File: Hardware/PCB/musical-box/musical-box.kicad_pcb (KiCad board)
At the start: 4 copper layers, 70 x 60 mm, 190 parts, among them J1 power, J201 PSU, J202 Jack-DC, J203 BATT, J401 SPI Display, J402 Rotary Encoder 1, J403 I2C Display, J404 Rotary Encoder 2, J405 WS2812, J501 spk_out, J502 aux in, J503 line in, P201 USB_C, P202 ICT-Point, P203 ICT-Point, P204 ICT-Point, Q201 IRFHM9331, Q204 IRF9362, Q301 BC846BDW1, SW301 boot, SW302 reset, U201 STUSB4500QTR, U202 MP2615, U203 TPS56339, U204 TLV75733PDBV, U205 TLV75733PDBV, U206 TLV803EC30DBZR, U301 CH340C, U302 ESP32-WROVER, U401 PCF8574ATS, U501 SPH0644HM4H-1, U502 SPH0644HM4H-1, U503 TAS5754MDCA

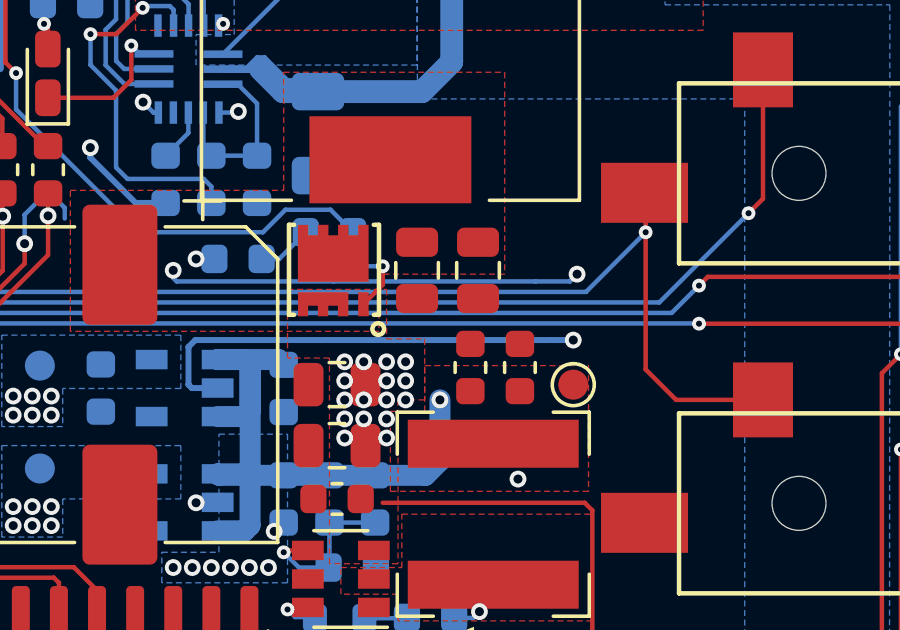
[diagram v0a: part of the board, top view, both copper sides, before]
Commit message: Fix error in schematic
The P-Channel MOSFet was connected in the wrong way, preventing the shutoff circuit from working properly
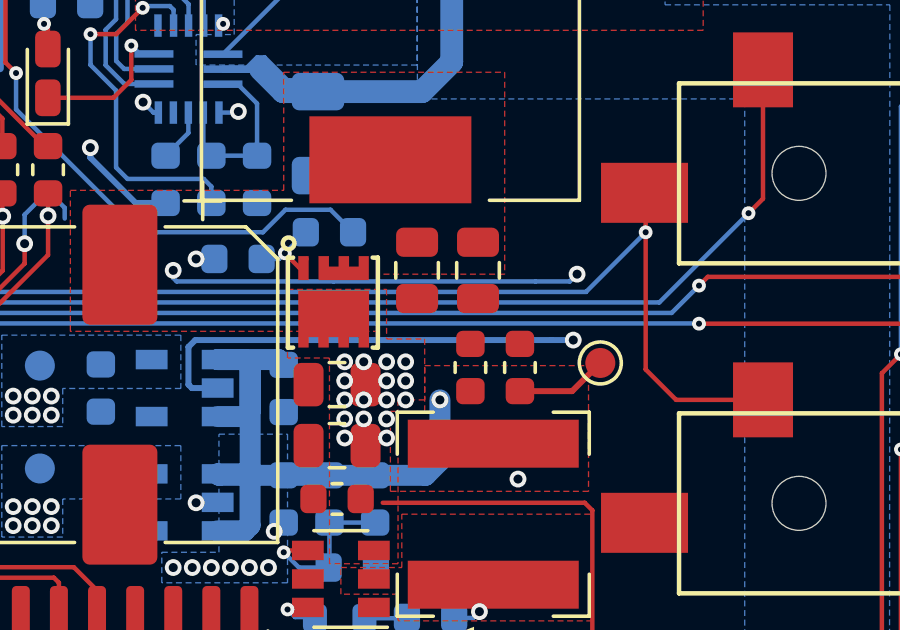
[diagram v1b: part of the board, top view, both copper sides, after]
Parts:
- R409: value 46.4k -> 46,4k
- moved P204 1.16 mm to (401.8, 155.3)
- moved Q201 0.29 mm to (392.9, 152.9), turned to 270 degrees
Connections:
- D202 pad 2: (no net) -> Net-(D202-Pad2)
- P201 pad A8: (no net) -> Net-(P201-PadA8)
- P201 pad B8: (no net) -> Net-(P201-PadB8)
- Q201 pad 2: +15V -> Net-(C201-Pad2)
- Q201 pad 3: Net-(C201-Pad2) -> +15V
- U201 pad 14: (no net) -> Net-(U201-Pad14)
- U201 pad 15: (no net) -> Net-(U201-Pad15)
- U201 pad 17: (no net) -> Net-(U201-Pad17)
- U201 pad 20: (no net) -> Net-(U201-Pad20)
- U201 pad 3: (no net) -> Net-(U201-Pad3)
- U202 pad 12: (no net) -> Net-(U202-Pad12)
- U203 pad 5: (no net) -> Net-(U203-Pad5)
- U301 pad 10: (no net) -> Net-(U301-Pad10)
- U301 pad 11: (no net) -> Net-(U301-Pad11)
- U301 pad 12: (no net) -> Net-(U301-Pad12)
- U301 pad 15: (no net) -> Net-(U301-Pad15)
- U301 pad 7: (no net) -> Net-(U301-Pad7)
- U301 pad 8: (no net) -> Net-(U301-Pad8)
- U301 pad 9: (no net) -> Net-(U301-Pad9)
- U302 pad 17: (no net) -> Net-(U302-Pad17)
- U302 pad 18: (no net) -> Net-(U302-Pad18)
- U302 pad 19: (no net) -> Net-(U302-Pad19)
- U302 pad 20: (no net) -> Net-(U302-Pad20)
- U302 pad 21: (no net) -> Net-(U302-Pad21)
- U302 pad 22: (no net) -> Net-(U302-Pad22)
- U401 pad 13: (no net) -> Net-(U401-Pad13)
- U401 pad 18: (no net) -> Net-(U401-Pad18)
- U401 pad 19: (no net) -> Net-(U401-Pad19)
- U401 pad 20: (no net) -> Net-(U401-Pad20)
- U401 pad 3: (no net) -> Net-(U401-Pad3)
- U401 pad 8: (no net) -> Net-(U401-Pad8)
- U503 pad 19: (no net) -> /Audio Output/GPIO1
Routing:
- net Net-(Q201-Pad1): track 6.92 -> 2.72 mm
- net +5V: track 82.1 -> 85.1 mm

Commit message: Addendum to 9e53ee1
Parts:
- C218, C222, C505, C506, C527, C528: value 22u -> 10u
- L203: value XAL6030-332MEB -> XAL6030-562
- R219: value 30.9k -> 52.3k
- R222, R312: value 10k -> 1k
- R302, R303: value 470R -> 220R
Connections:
- Q204 pad 1: Net-(Q204-Pad1) -> Net-(C204-Pad1)
- Q204 pad 3: Net-(Q204-Pad1) -> Net-(C204-Pad1)
- R204 pad 1: Net-(Q204-Pad1) -> Net-(C204-Pad1)
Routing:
- net Net-(C204-Pad1): track 1.11 -> 8.51 mm, vias 1 -> 2
- net Net-(Q204-Pad1): track 2.05 -> 0.00 mm, vias 1 -> 0
- net GND: track 309.4 -> 310.8 mm
- added copper zone on F.Cu, net Net-(C204-Pad1)
- removed copper zone on F.Cu, net Net-(Q204-Pad1)

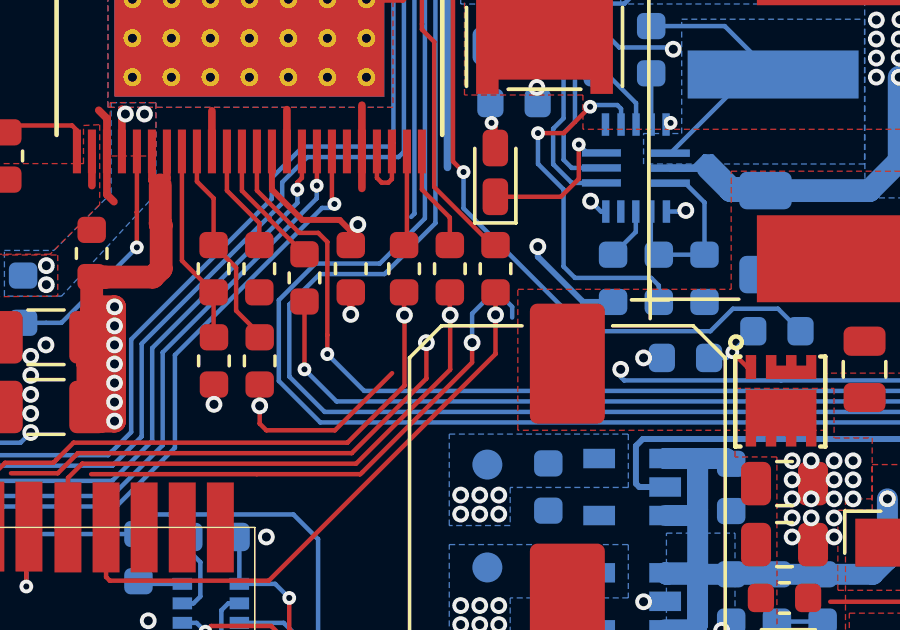
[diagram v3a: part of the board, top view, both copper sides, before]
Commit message: Remove needless vias
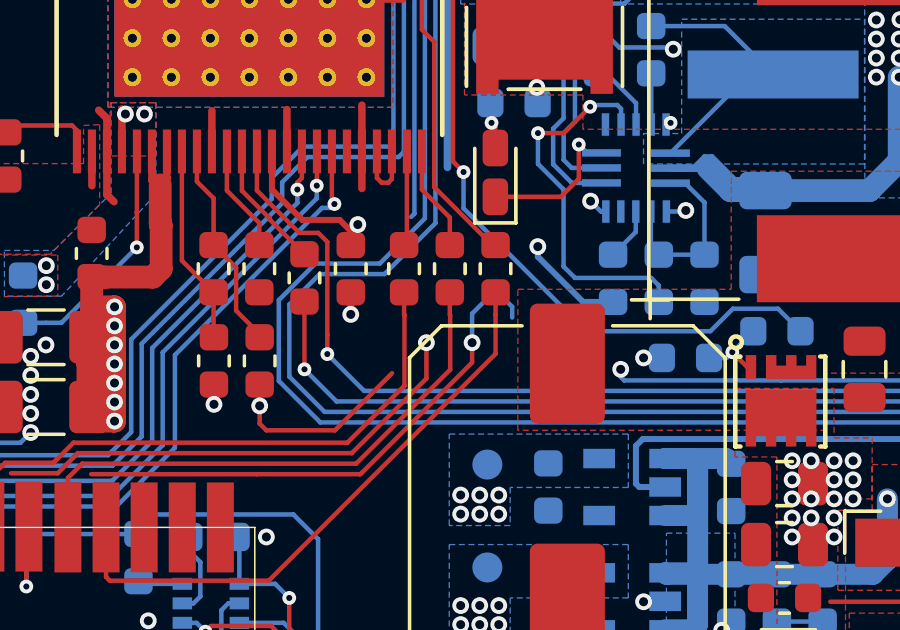
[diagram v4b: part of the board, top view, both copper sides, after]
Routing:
- net /Microcontroller/IO15: vias 1 -> 0
- net /Microcontroller/IO04: vias 1 -> 0
- net /Microcontroller/IO02: vias 1 -> 0

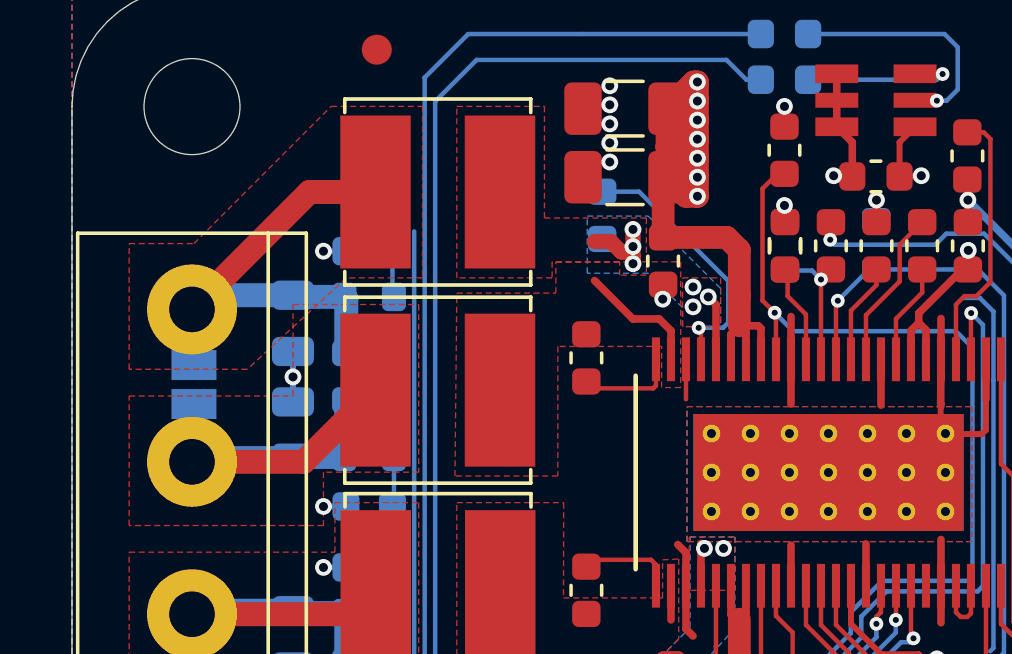
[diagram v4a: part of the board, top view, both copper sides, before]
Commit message: Bugfix: Fix speaker B connection to make the output work
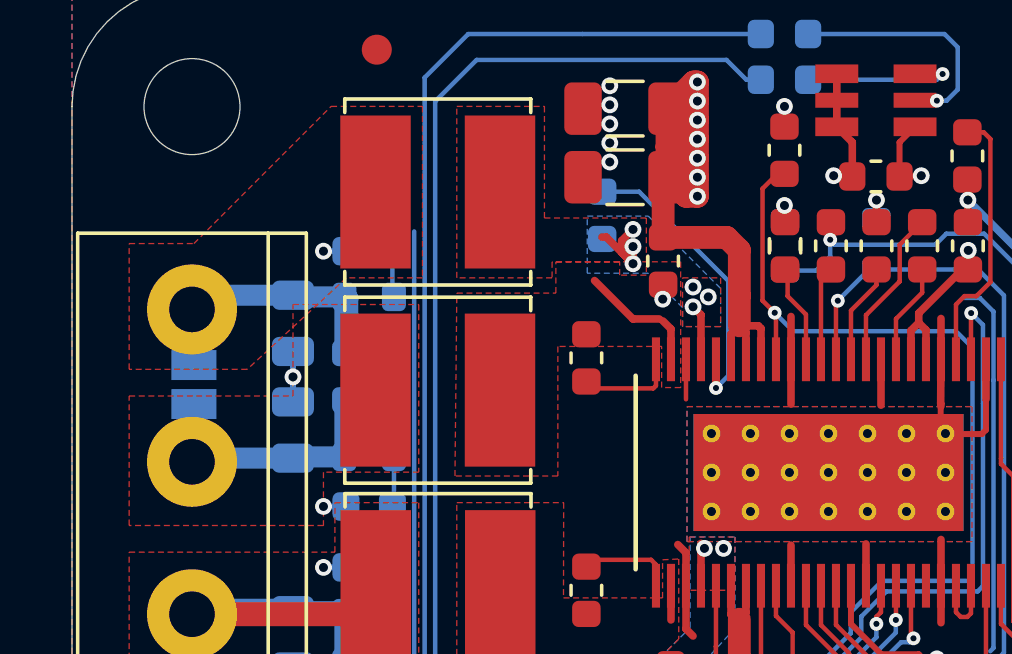
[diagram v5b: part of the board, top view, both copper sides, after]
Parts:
- R508: value 46.4k -> 10k
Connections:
- C515 pad 1: /Audio Output/SPKB_OUT+ -> /Audio Output/SPKB_OUT-
- C516 pad 1: /Audio Output/OUT2+ -> /Audio Output/OUT2-
- C519 pad 1: /Audio Output/OUT2+ -> /Audio Output/OUT2-
- C519 pad 2: /Audio Output/OUT2- -> /Audio Output/OUT2+
- C520 pad 1: /Audio Output/SPKB_OUT- -> /Audio Output/SPKB_OUT+
- C523 pad 1: /Audio Output/OUT2- -> /Audio Output/OUT2+
- C525 pad 1: /Audio Output/SPK_INB+ -> Net-(C525-Pad1)
- C525 pad 2: Net-(C525-Pad2) -> /Audio Output/SPK_INB+
- J501 pad 3: /Audio Output/OUT2+ -> /Audio Output/OUT2-
- J501 pad 4: /Audio Output/OUT2- -> /Audio Output/OUT2+
- J502 pad R1: Net-(C525-Pad2) -> /Audio Output/SPK_INB+
- JP4 pad 1: /Audio Output/OUT2+ -> /Audio Output/OUT2-
- JP4 pad 2: /Audio Output/OUT2- -> /Audio Output/OUT2+
- L503 pad 1: /Audio Output/SPKB_OUT+ -> /Audio Output/SPKB_OUT-
- L503 pad 2: /Audio Output/OUT2+ -> /Audio Output/OUT2-
- L504 pad 1: /Audio Output/SPKB_OUT- -> /Audio Output/SPKB_OUT+
- L504 pad 2: /Audio Output/OUT2- -> /Audio Output/OUT2+
- R510 pad 2: /Audio Output/OUT2+ -> /Audio Output/OUT2-
- R511 pad 2: /Audio Output/OUT2- -> /Audio Output/OUT2+
- U503 pad 37: /Audio Output/SPK_INB+ -> Net-(C525-Pad1)
- U503 pad 44: /Audio Output/SPKB_OUT- -> Net-(C520-Pad2)
- U503 pad 45: Net-(C520-Pad2) -> /Audio Output/SPKB_OUT+
- U503 pad 47: /Audio Output/SPKB_OUT+ -> /Audio Output/SPKB_OUT-
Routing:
- net Net-(C525-Pad2): track 68.0 -> 0.00 mm, vias 2 -> 0
- net /Audio Output/SPK_INB+: track 4.45 -> 70.3 mm, vias 1 -> 2
- net /Audio Output/OUT2-: track 16.8 -> 9.01 mm
- net /Audio Output/OUT2+: track 16.1 -> 9.08 mm
- net Net-(C525-Pad1): track 0.00 -> 3.13 mm
- net /Audio Output/SPKB_OUT+: track 4.19 -> 6.74 mm, vias 0 -> 6
- net /Audio Output/SPKB_OUT-: track 6.50 -> 4.08 mm, vias 6 -> 0
- net Net-(C520-Pad2): track 8.96 -> 10.1 mm
- added copper zone on B.Cu, net /Audio Output/SPKB_OUT+
- removed copper zone on B.Cu, net /Audio Output/SPKB_OUT-

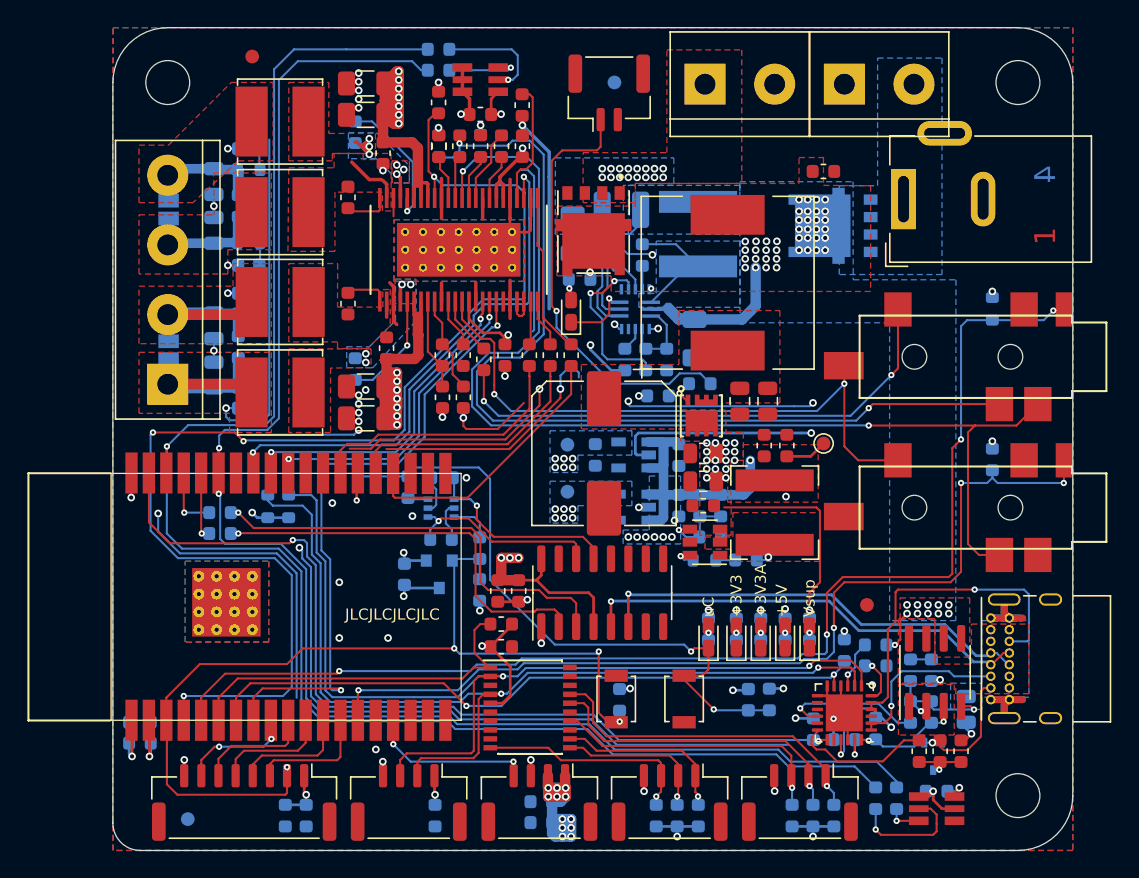
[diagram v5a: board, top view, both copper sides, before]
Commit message: Reduce part count on the USB PD device and add some ESD protection
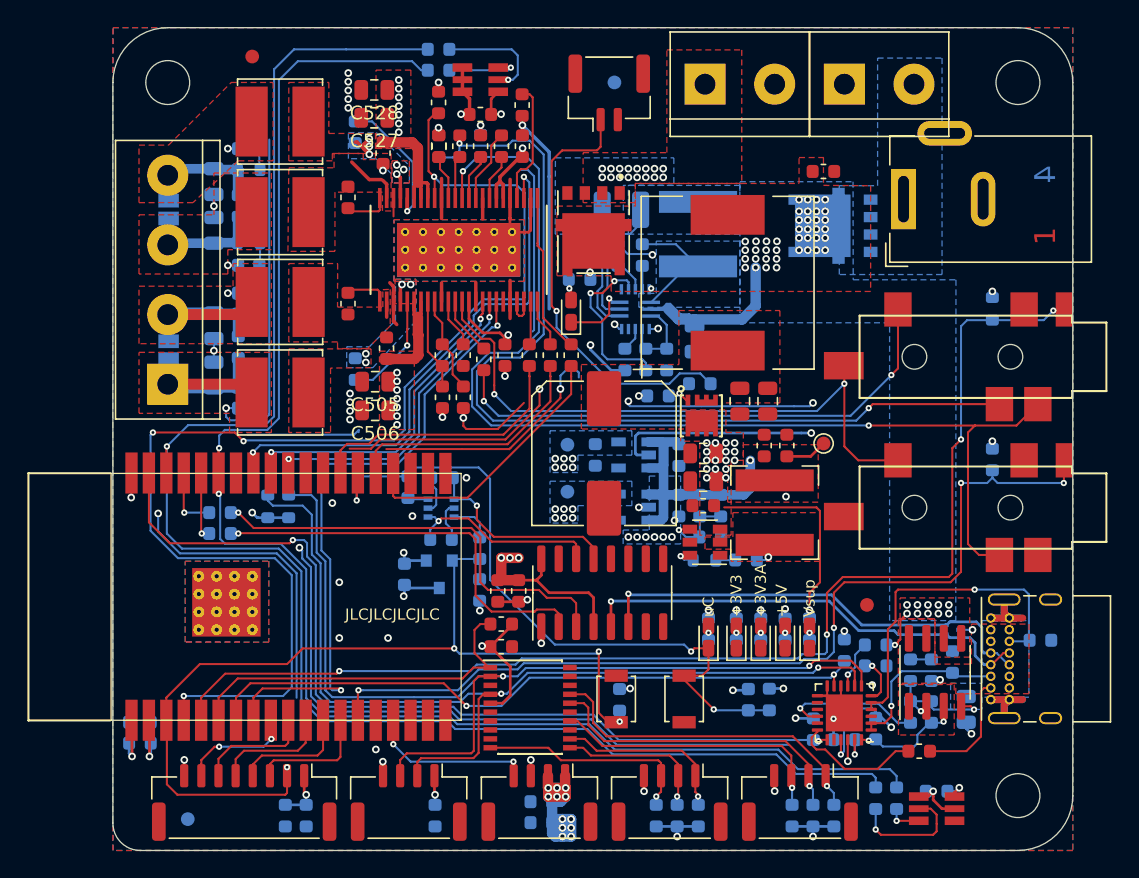
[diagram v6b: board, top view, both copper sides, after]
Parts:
- removed C210: 100n, Capacitor_SMD:C_0603_1608Metric
- removed R203: 470, Resistor_SMD:R_0603_1608Metric
- added D206: 24V, Diode_SMD:D_0603_1608Metric, B.Cu at (411.2, 171.3)
- added U207: TPD2EUSB30A, Package_TO_SOT_SMD:Texas_DRT-3, B.Cu at (411.2, 168.9)
- C211, C212: value 22u -> 10u; footprint Capacitor_SMD:C_1206_3216Metric -> Capacitor_SMD:C_0805_2012Metric
- C505, C506, C527, C528: footprint Capacitor_SMD:C_1206_3216Metric -> Capacitor_SMD:C_0805_2012Metric
- D202: value BAT54W -> 24V; footprint Package_TO_SOT_SMD:SOT-323_SC-70 -> Diode_SMD:D_0603_1608Metric
- R202: value 470k -> 100k
- R209, R216: value 100k -> 10k
- moved D202 11.5 mm to (417.6, 169.7), turned to 0 degrees
- moved C506 0.90 mm to (369.1, 152.9)
- moved C528 0.79 mm to (369.1, 129.5)
- moved C505 0.78 mm to (369.1, 150.8)
- moved C527 0.66 mm to (369.1, 131.6)
- turned R207 to 180 degrees
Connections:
- D202 pad 1: Net-(C203-Pad2) -> Net-(D202-Pad1)
- D202 pad 2: Net-(D202-Pad2) -> GND
- P201 pad B5: Net-(P201-PadB5) -> Net-(D202-Pad1)
- R207 pad 1: Net-(C210-Pad2) -> Net-(C203-Pad2)
- U201 pad 22: GND -> +3V3
- U201 pad 4: Net-(P201-PadB5) -> Net-(D202-Pad1)
- U201 pad 5: Net-(P201-PadB5) -> Net-(D202-Pad1)
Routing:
- net +15V: track 69.1 -> 33.3 mm
- net Net-(P201-PadB5): track 24.5 -> 0.00 mm, vias 1 -> 0
- net Net-(D202-Pad1): track 0.00 -> 24.5 mm, vias 0 -> 1
- net Net-(C210-Pad2): track 4.09 -> 0.00 mm, vias 1 -> 0
- net +3V3: track 183.2 -> 184.8 mm, vias 27 -> 28
- net /Microcontroller/D-: track 32.5 -> 33.6 mm
- net Net-(C203-Pad2): track 9.30 -> 8.29 mm, vias 1 -> 0
- net GND: track 310.8 -> 309.9 mm, vias 63 -> 62
- net Net-(R207-Pad2): track 10.2 -> 9.57 mm
- net /Microcontroller/D+: track 33.2 -> 33.7 mm
